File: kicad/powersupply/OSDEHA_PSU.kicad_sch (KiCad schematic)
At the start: 62 parts, among them J1 340 VAC / 220 mA, J10 HEATERS-LEFT, J11 HEATERS-RIGHT, J12 COLEMANREG-LEFT-1, J13 COLEMANREG-LEFT-2, J14 COLEMANREG-RIGHT-1, J15 COLEMANREG-RIGHT-2, J2 340 VAC / 220 mA, J3 420 VAC / 75 mA, J4 9 VAC / 4.5 A, J5 10.5 VAC / 4.5 A, J6 10.5 VAC / 4.5 A, J7 Stator bias, J8 HV-L, J9 HV-R, K1 RT424006, Q1 BD138, Q2 10M90S, U1 LM1085-ADJ, U2 NE555P

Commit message: psu
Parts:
- C7: value 10u 16 V -> 22u 16 V; MPN 860160372001 -> 860160372003
- D5, D7: footprint Diode_THT:D_DO-41_SOD81_P10.16mm_Horizontal -> Diode_THT:D_DO-41_SOD81_P7.62mm_Horizontal
- R12, R13, R4: footprint Resistor_THT:R_Axial_DIN0207_L6.3mm_D2.5mm_P10.16mm_Horizontal -> Resistor_THT:R_Axial_DIN0207_L6.3mm_D2.5mm_P2.54mm_Vertical
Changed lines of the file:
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@@
       (effects (font (size 1.27 1.27)))
     )
-    (property "Footprint" "Resistor_THT:R_Axial_DIN0207_L6.3mm_D2.5mm_P10.16mm_Horizontal" (at 187.452 57.15 90)
+    (property "Footprint" "Resistor_THT:R_Axial_DIN0207_L6.3mm_D2.5mm_P2.54mm_Vertical" (at 187.452 57.15 90)
       (effects (font (size 1.27 1.27)) hide)
     )
@@
         (path "/ca37e2fa-48ac-4eb3-a7a4-1e3bbee61661"
           (reference "Q2") (unit 1)
-        )
-      )
-    )
-  )
-  (symbol (lib_id "Device:C_Polarized") (at 137.16 232.41 0) (unit 1)
-    (in_bom yes) (on_board yes) (dnp no) (fields_autoplaced)
-    (property "Reference" "C7" (at 140.97 230.251 0)
-      (effects (font (size 1.27 1.27)) (justify left))
-    )
-    (property "Value" "10u 16 V" (at 140.97 232.791 0)
-      (effects (font (size 1.27 1.27)) (justify left))
-    )
-    (property "Footprint" "Capacitor_THT:CP_Radial_D5.0mm_P2.00mm" (at 138.1252 236.22 0)
-      (effects (font (size 1.27 1.27)) hide)
-    )
-    (property "Datasheet" "https://www.we-online.com/catalog/datasheet/860160372001.pdf" (at 137.16 232.41 0)
-      (effects (font (size 1.27 1.27)) hide)
-    )
-    (property "MPN" "860160372001 " (at 137.16 232.41 0)
-      (effects (font (size 1.27 1.27)) hide)
-    )
-    (pin "1")
-    (pin "2")
-    (instances
-      (project "OSDEHA_PSU"
-        (path "/ca37e2fa-48ac-4eb3-a7a4-1e3bbee61661"
-          (reference "C7") (unit 1)
         )
       )
@@
     )
   )
+  (symbol (lib_id "Device:C_Polarized") (at 137.16 232.41 0) (unit 1)
+    (in_bom yes) (on_board yes) (dnp no)
+    (property "Reference" "C7" (at 140.97 236.22 0)
+      (effects (font (size 1.27 1.27)))
+    )
+    (property "Value" "22u 16 V" (at 147.32 232.41 0)
+      (effects (font (size 1.27 1.27)))
+    )
+    (property "Footprint" "Capacitor_THT:CP_Radial_D5.0mm_P2.00mm" (at 138.1252 236.22 0)
+      (effects (font (size 1.27 1.27)) hide)
+    )
+    (property "Datasheet" "https://www.we-online.com/catalog/datasheet/860160372003.pdf" (at 137.16 232.41 0)
+      (effects (font (size 1.27 1.27)) hide)
+    )
+    (property "MPN" "860160372003 " (at 137.16 232.41 90)
+      (effects (font (size 1.27 1.27)) hide)
+    )
+    (pin "1")
+    (pin "2")
+    (instances
+      (project "OSDEHA_PSU"
+        (path "/ca37e2fa-48ac-4eb3-a7a4-1e3bbee61661"
+          (reference "C7") (unit 1)
+        )
+      )
+    )
+  )
   (symbol (lib_id "Device:R") (at 120.65 237.49 0) (unit 1)
     (in_bom yes) (on_board yes) (dnp no)
@@
       (effects (font (size 1.27 1.27)))
     )
-    (property "Footprint" "Resistor_THT:R_Axial_DIN0207_L6.3mm_D2.5mm_P10.16mm_Horizontal" (at 94.742 232.41 90)
+    (property "Footprint" "Resistor_THT:R_Axial_DIN0207_L6.3mm_D2.5mm_P2.54mm_Vertical" (at 94.742 232.41 90)
       (effects (font (size 1.27 1.27)) hide)
     )
@@
       (effects (font (size 1.27 1.27)))
     )
-    (property "Footprint" "Resistor_THT:R_Axial_DIN0207_L6.3mm_D2.5mm_P10.16mm_Horizontal" (at 198.882 57.15 90)
+    (property "Footprint" "Resistor_THT:R_Axial_DIN0207_L6.3mm_D2.5mm_P2.54mm_Vertical" (at 198.882 57.15 90)
       (effects (font (size 1.27 1.27)) hide)
     )
@@
       (effects (font (size 1.27 1.27)))
     )
-    (property "Footprint" "Diode_THT:D_DO-41_SOD81_P10.16mm_Horizontal" (at 123.19 48.895 0)
+    (property "Footprint" "Diode_THT:D_DO-41_SOD81_P7.62mm_Horizontal" (at 123.19 48.895 0)
       (effects (font (size 1.27 1.27)) hide)
     )
@@
       (effects (font (size 1.27 1.27)))
     )
-    (property "Footprint" "Diode_THT:D_DO-41_SOD81_P10.16mm_Horizontal" (at 113.03 48.895 0)
-      (effects (font (size 1.27 1.27)) hide)
-    )
+    (property "Footprint" "Diode_THT:D_DO-41_SOD81_P7.62mm_Horizontal" (at 113.03 48.895 0)
+      (effects (font (size 1.27 1.27)) hide)
+    )

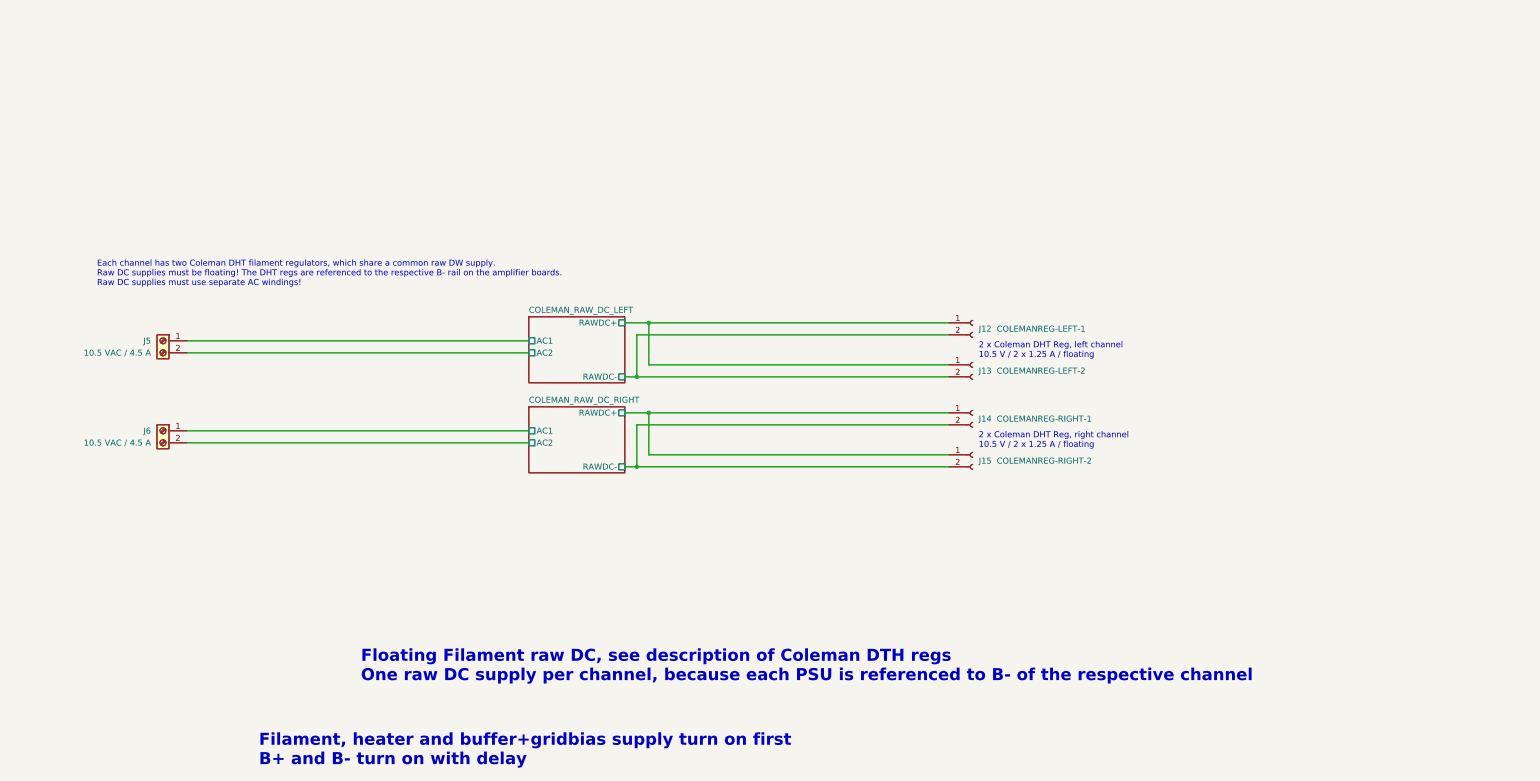
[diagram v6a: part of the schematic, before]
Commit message: move coleman reg psu to separate board
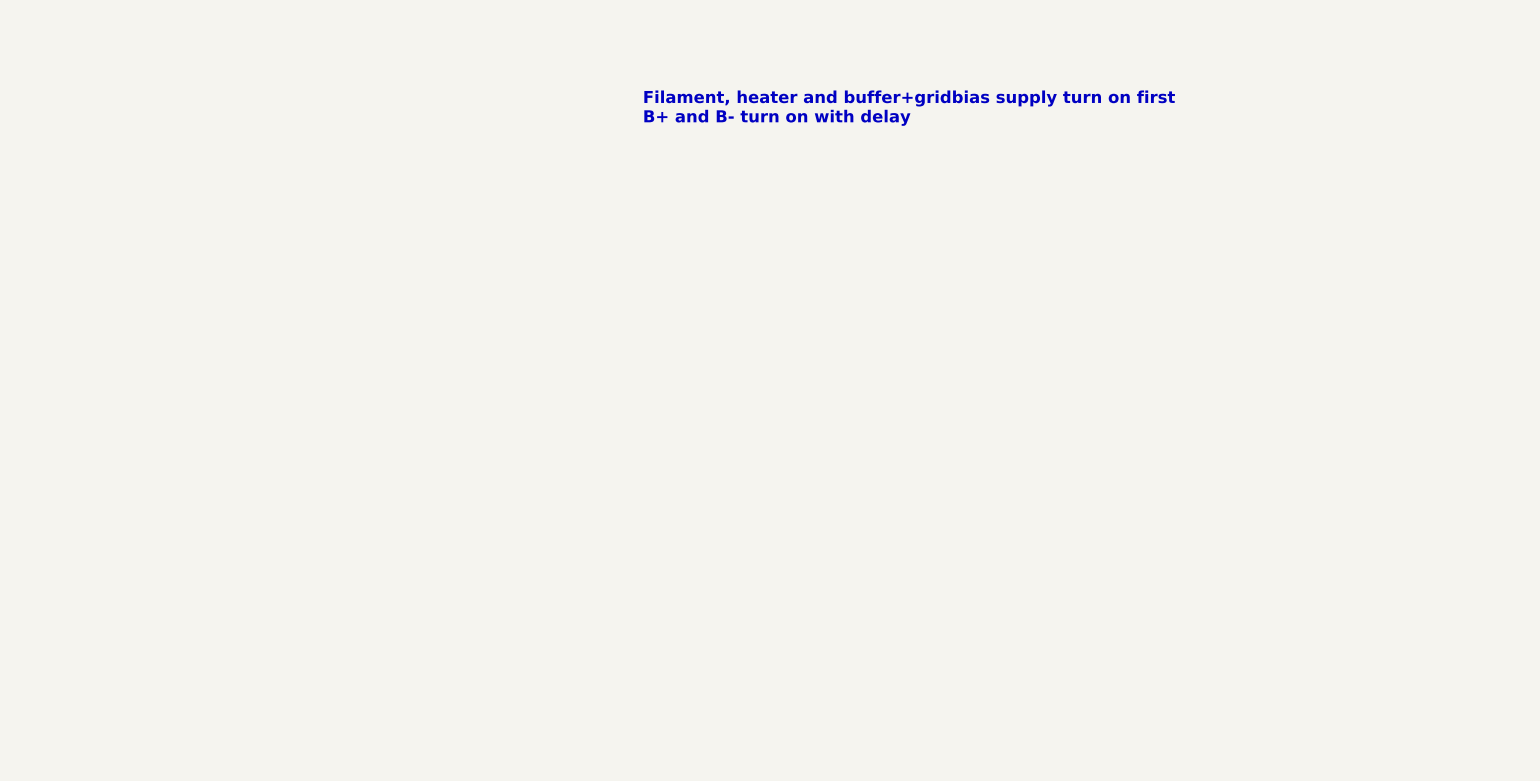
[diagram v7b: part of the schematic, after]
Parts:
- removed J12: COLEMANREG-LEFT-1, Connector_Molex:Molex_KK-396_A-41791-0002_1x02_P3.96mm_Vertical, symbol Connector:Conn_01x02_Socket
- removed J13: COLEMANREG-LEFT-2, Connector_Molex:Molex_KK-396_A-41791-0002_1x02_P3.96mm_Vertical, symbol Connector:Conn_01x02_Socket
- removed J14: COLEMANREG-RIGHT-1, Connector_Molex:Molex_KK-396_A-41791-0002_1x02_P3.96mm_Vertical, symbol Connector:Conn_01x02_Socket
- removed J15: COLEMANREG-RIGHT-2, Connector_Molex:Molex_KK-396_A-41791-0002_1x02_P3.96mm_Vertical, symbol Connector:Conn_01x02_Socket
- removed J5, J6: 10.5 VAC / 4.5 A, TerminalBlock_Phoenix:TerminalBlock_Phoenix_MKDS-1,5-2-5.08_1x02_P5.08mm_Horizontal, symbol Connector:Screw_Terminal_01x02
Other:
- removed sheet COLEMAN_RAW_DC_LEFT
- removed sheet COLEMAN_RAW_DC_RIGHT
- note removed: "2 x Coleman DHT Reg, left channel 10.5 V / 2 x 1.25 A / floating"
- note removed: "2 x Coleman DHT Reg, right channel 10.5 V / 2 x 1.25 A / floating"
- note removed: "Each channel has two Coleman DHT filament regulators, which share a common raw DW supply. Raw DC supplies must be floating! The DHT regs are referenced to the respective B- rail on the amplifier boards. Raw DC supplies must use separate AC windings!"
- note removed: "Floating Filament raw DC, see description of Coleman DTH regs One raw DC supply per channel, because each PSU is referenced to B- of the respective channel"

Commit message: psu
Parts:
- renumbered J7 to J5, J8 to J6, J9 to J7, J10 to J8, J11 to J9
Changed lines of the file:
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@@
   (symbol (lib_id "Connector:Conn_01x02_Socket") (at 218.44 241.3 0) (unit 1)
     (in_bom yes) (on_board yes) (dnp no) (fields_autoplaced)
-    (property "Reference" "J11" (at 219.71 241.3 0)
+    (property "Reference" "J9" (at 219.71 241.3 0)
       (effects (font (size 1.27 1.27)) (justify left))
     )
@@
       (project "OSDEHA_PSU"
         (path "/ca37e2fa-48ac-4eb3-a7a4-1e3bbee61661"
-          (reference "J11") (unit 1)
+          (reference "J9") (unit 1)
         )
       )
@@
   (symbol (lib_id "Connector:Conn_01x04_Socket") (at 218.44 116.84 0) (unit 1)
     (in_bom yes) (on_board yes) (dnp no)
-    (property "Reference" "J9" (at 219.71 118.11 0)
+    (property "Reference" "J7" (at 219.71 118.11 0)
       (effects (font (size 1.27 1.27)) (justify left))
     )
@@
       (project "OSDEHA_PSU"
         (path "/ca37e2fa-48ac-4eb3-a7a4-1e3bbee61661"
-          (reference "J9") (unit 1)
+          (reference "J7") (unit 1)
         )
       )
@@
   (symbol (lib_id "Connector:Conn_01x02_Socket") (at 218.44 53.34 0) (unit 1)
     (in_bom yes) (on_board yes) (dnp no)
-    (property "Reference" "J7" (at 219.71 54.61 0)
+    (property "Reference" "J5" (at 219.71 54.61 0)
       (effects (font (size 1.27 1.27)) (justify left))
     )
@@
       (project "OSDEHA_PSU"
         (path "/ca37e2fa-48ac-4eb3-a7a4-1e3bbee61661"
-          (reference "J7") (unit 1)
+          (reference "J5") (unit 1)
         )
       )
@@
   (symbol (lib_id "Connector:Conn_01x02_Socket") (at 218.44 222.25 0) (unit 1)
     (in_bom yes) (on_board yes) (dnp no) (fields_autoplaced)
-    (property "Reference" "J10" (at 219.71 222.25 0)
+    (property "Reference" "J8" (at 219.71 222.25 0)
       (effects (font (size 1.27 1.27)) (justify left))
     )
@@
       (project "OSDEHA_PSU"
         (path "/ca37e2fa-48ac-4eb3-a7a4-1e3bbee61661"
-          (reference "J10") (unit 1)
+          (reference "J8") (unit 1)
         )
       )
@@
   (symbol (lib_id "Connector:Conn_01x04_Socket") (at 218.44 83.82 0) (unit 1)
     (in_bom yes) (on_board yes) (dnp no)
-    (property "Reference" "J8" (at 219.71 85.09 0)
+    (property "Reference" "J6" (at 219.71 85.09 0)
       (effects (font (size 1.27 1.27)) (justify left))
     )
@@
       (project "OSDEHA_PSU"
         (path "/ca37e2fa-48ac-4eb3-a7a4-1e3bbee61661"
-          (reference "J8") (unit 1)
-        )
-      )
+          (reference "J6") (unit 1)
+        )
+      )
